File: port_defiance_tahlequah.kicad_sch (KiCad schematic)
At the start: 7 parts

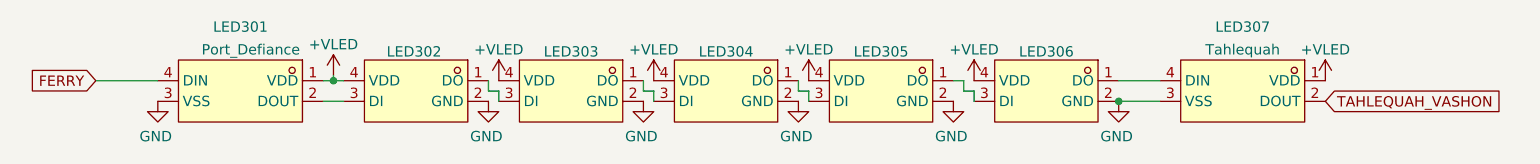
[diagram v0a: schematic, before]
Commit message: Replace ferry port LED
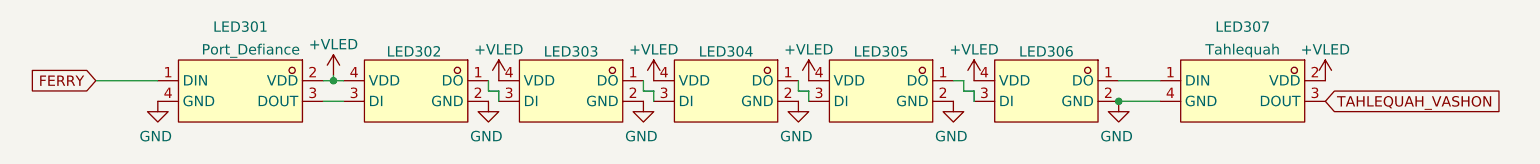
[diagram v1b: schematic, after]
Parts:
- LED301, LED307: value WS2812B-Mini -> WS2812B-MINI-X2; footprint EasyEDA:LED-SMD_4P-L3.5-W3.5-TL_WS2812B -> EasyEDA:LED-SMD_4P-L3.5-W3.5-TL_WS2812B-MINI-X2; symbol EasyEDA:WS2812B-MINI -> EasyEDA:WS2812B-MINI-X2; LCSC Part C527089 -> C4154873
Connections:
- net +VLED: now also LED301.2 (VDD), LED307.2 (VDD); no longer LED301.1 (VDD), LED307.1 (VDD)
- net FERRY: now also LED301.1 (DIN); no longer LED301.4 (DIN)
- net GND: now also LED301.4 (GND), LED307.4 (GND); no longer LED301.3 (VSS), LED307.3 (VSS)
- net TAHLEQUAH_VASHON: now also LED307.3 (DOUT); no longer LED307.2 (DOUT)
- net at LED302.3 (DI): now also LED301.3 (DOUT); no longer LED301.2 (DOUT)
- net at LED306.1 (DO): now also LED307.1 (DIN); no longer LED307.4 (DIN)
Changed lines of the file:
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@@
 	)
 	(symbol
-		(lib_id "EasyEDA:WS2812B-MINI")
+		(lib_id "EasyEDA:WS2812B-MINI-X2")
 		(at 86.36 41.91 0)
 		(mirror y)
@@
 			)
 		)
-		(property "Value" "WS2812B-Mini"
+		(property "Value" "WS2812B-MINI-X2"
 			(at 76.2 40.386 0)
 			(hide yes)
@@
 			)
 		)
-		(property "Footprint" "EasyEDA:LED-SMD_4P-L3.5-W3.5-TL_WS2812B"
+		(property "Footprint" "EasyEDA:LED-SMD_4P-L3.5-W3.5-TL_WS2812B-MINI-X2"
 			(at 86.36 54.61 0)
 			(hide yes)
@@
 			)
 		)
-		(property "Datasheet" "https://lcsc.com/product-detail/Light-Emitting-Diodes-LED_Worldsemi-WS2812B-Mini_C527089.html"
+		(property "Datasheet" "https://www.lcsc.com/datasheet/C4154873.pdf"
 			(at 86.36 57.15 0)
 			(hide yes)
@@
 			)
 		)
-		(property "Description" ""
+		(property "Description" "Worldsemi WS2812B-MINI-X2 addressable RGB LED, 3.5 x 3.5 x 0.95 mm"
 			(at 86.36 41.91 0)
 			(hide yes)
@@
 			)
 		)
-		(property "LCSC Part" "C527089"
+		(property "LCSC Part" "C4154873"
 			(at 86.36 59.69 0)
 			(hide yes)
@@
 			)
 		)
+		(pin "2"
+		)
 		(pin "1"
 		)
+		(pin "3"
+		)
 		(pin "4"
-		)
-		(pin "2"
-		)
-		(pin "3"
 		)
 		(instances
@@
 	)
 	(symbol
-		(lib_id "EasyEDA:WS2812B-MINI")
+		(lib_id "EasyEDA:WS2812B-MINI-X2")
 		(at 209.55 41.91 0)
 		(mirror y)
@@
 			)
 		)
-		(property "Value" "WS2812B-Mini"
+		(property "Value" "WS2812B-MINI-X2"
 			(at 199.39 40.386 0)
 			(hide yes)
@@
 			)
 		)
-		(property "Footprint" "EasyEDA:LED-SMD_4P-L3.5-W3.5-TL_WS2812B"
+		(property "Footprint" "EasyEDA:LED-SMD_4P-L3.5-W3.5-TL_WS2812B-MINI-X2"
 			(at 209.55 54.61 0)
 			(hide yes)
@@
 			)
 		)
-		(property "Datasheet" "https://lcsc.com/product-detail/Light-Emitting-Diodes-LED_Worldsemi-WS2812B-Mini_C527089.html"
+		(property "Datasheet" "https://www.lcsc.com/datasheet/C4154873.pdf"
 			(at 209.55 57.15 0)
 			(hide yes)
@@
 			)
 		)
-		(property "Description" ""
+		(property "Description" "Worldsemi WS2812B-MINI-X2 addressable RGB LED, 3.5 x 3.5 x 0.95 mm"
 			(at 209.55 41.91 0)
 			(hide yes)
@@
 			)
 		)
-		(property "LCSC Part" "C527089"
+		(property "LCSC Part" "C4154873"
 			(at 209.55 59.69 0)
 			(hide yes)
@@
 			)
 		)
+		(pin "2"
+		)
 		(pin "1"
 		)
+		(pin "3"
+		)
 		(pin "4"
 		)
-		(pin "2"
-		)
-		(pin "3"
-		)
 		(instances
